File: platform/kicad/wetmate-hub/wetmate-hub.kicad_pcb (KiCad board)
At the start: 2 copper layers, 20.5 x 19.4 mm, 2 parts, among them J1 Screw_Terminal_01x04, J2 Screw_Terminal_01x02

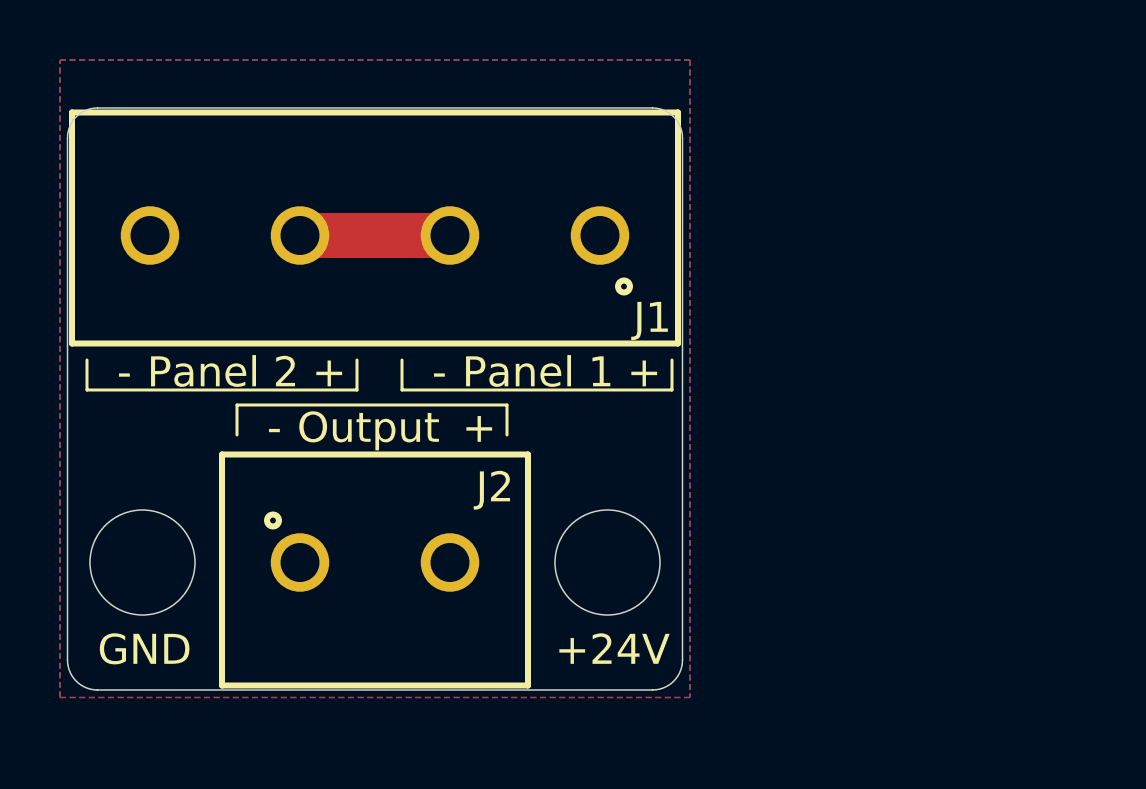
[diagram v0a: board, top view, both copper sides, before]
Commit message: Wetmate Hub: Finalise layout for production
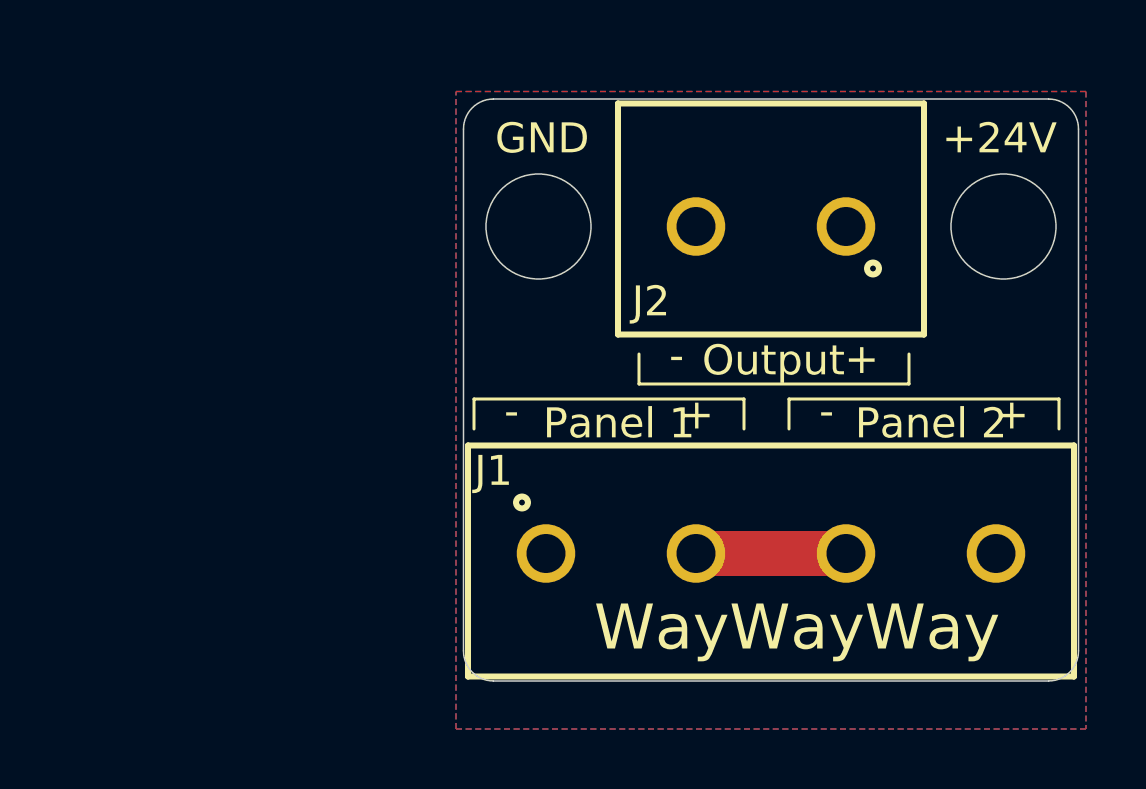
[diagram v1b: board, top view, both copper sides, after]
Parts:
- moved J2 17.3 mm to (123.3, 75.0), turned to 180 degrees
- moved J1 16.9 mm to (123.3, 85.8), turned to 0 degrees
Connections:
- J1 pad 1: /24V -> /GND
- J1 pad 4: /GND -> /24V
- J2 pad 1: /GND -> /24V
- J2 pad 2: /24V -> /GND
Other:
- outline, holes or cut-outs redrawn
- board text added: "WayWayWay"
